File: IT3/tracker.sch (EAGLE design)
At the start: 91 parts, among them J1 THING_PLUS_PHYSICAL, Q1 2N3906, Q2 DMG6602SVT, Q3 DMG6602SVT, Q6 MMBT3906LT1SMD, Q7 DMG6602SVT, U1 ADXL343BCCZ-RL7, U2 FONA-800-BREAKOUTNOHOLE, U3 MP2155GQ-Z, U4 SPARKFUN-SWARM-M138NOTOPHOLE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

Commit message: Update 4V PSUvalues
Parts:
- R10: value 143k -> 121k
- R9: value 820k -> 845k
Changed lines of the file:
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@@
 <attribute name="VOLTAGE_RATING" value="50V"/>
 </part>
-<part name="R9" library="SparkFun-Resistors" deviceset="RESISTOR" device="0603" value=" 820k">
+<part name="R9" library="SparkFun-Resistors" deviceset="RESISTOR" device="0603" value=" 845k">
 <attribute name="TOLERANCE" value="1%"/>
 </part>
-<part name="R10" library="SparkFun-Resistors" deviceset="RESISTOR" device="0603" value="143k">
+<part name="R10" library="SparkFun-Resistors" deviceset="RESISTOR" device="0603" value="121k">
 <attribute name="TOLERANCE" value="1%"/>
 </part>

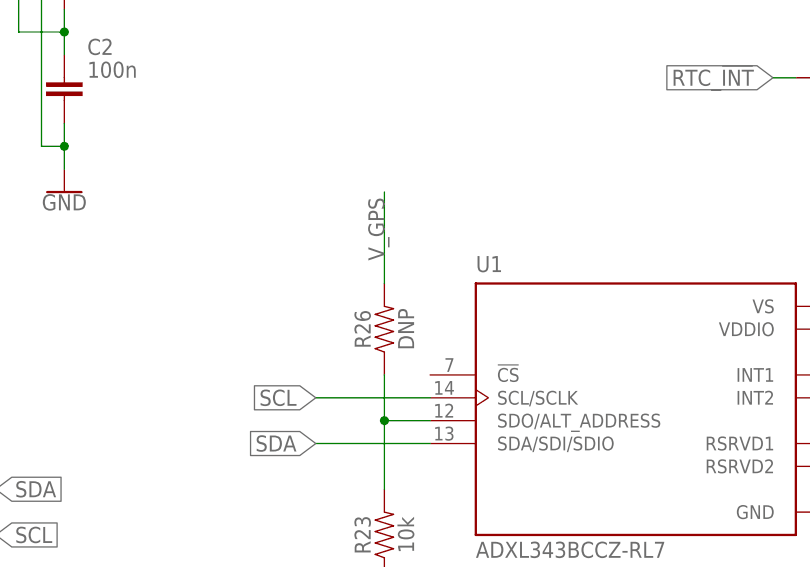
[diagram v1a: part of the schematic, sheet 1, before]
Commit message: Fixes for accelerometer CS pullup
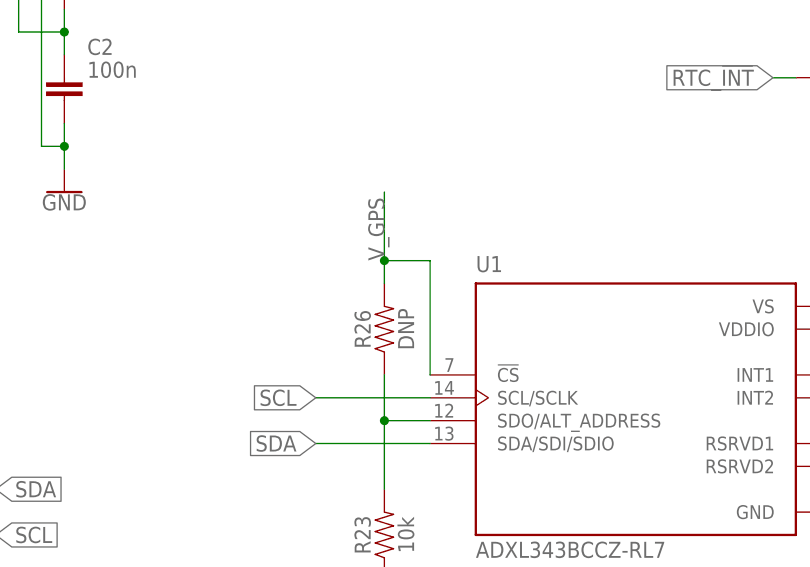
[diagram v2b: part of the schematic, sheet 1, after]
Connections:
- net V_GPS: now also U1.!CS
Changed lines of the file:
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@@
 </segment>
 <segment>
-<wire x1="129.54" y1="81.28" x2="129.54" y2="71.12" width="0.1524" layer="91"/>
+<wire x1="129.54" y1="81.28" x2="129.54" y2="73.66" width="0.1524" layer="91"/>
 <label x="129.54" y="73.66" size="1.778" layer="95" rot="R90"/>
 <pinref part="R26" gate="G$1" pin="2"/>
+<pinref part="U1" gate="G$1" pin="!CS"/>
+<wire x1="129.54" y1="73.66" x2="129.54" y2="71.12" width="0.1524" layer="91"/>
+<wire x1="134.62" y1="60.96" x2="134.62" y2="73.66" width="0.1524" layer="91"/>
+<wire x1="134.62" y1="73.66" x2="129.54" y2="73.66" width="0.1524" layer="91"/>
+<junction x="129.54" y="73.66"/>
 </segment>
 </net>

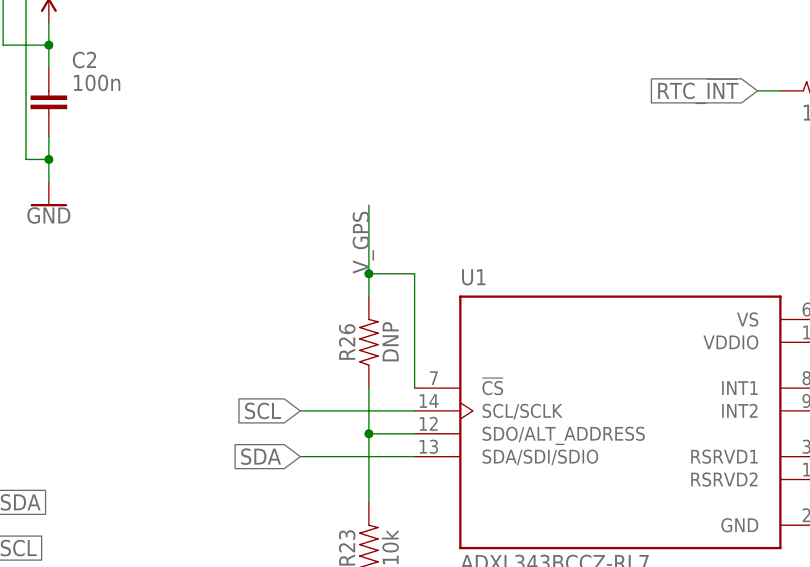
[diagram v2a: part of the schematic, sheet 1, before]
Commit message: Properly fix the accelerometer issue and move the GPS power FET slightly
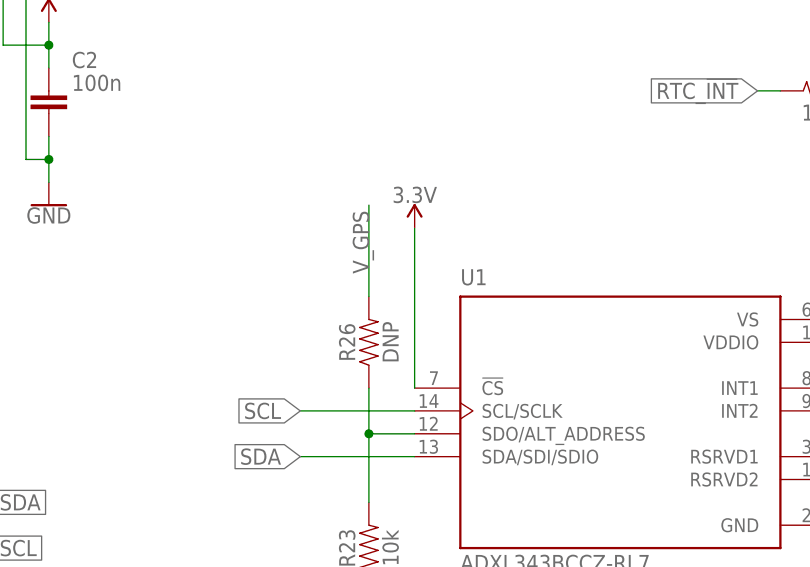
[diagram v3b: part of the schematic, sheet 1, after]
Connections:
- net 3.3V: now also U1.!CS
- net V_GPS: no longer U1.!CS
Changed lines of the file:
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@@
 <part name="GND38" library="SparkFun-PowerSymbols" deviceset="GND" device=""/>
 <part name="U$2" library="GlacTracker" deviceset="SLOT130.5" device=""/>
+<part name="SUPPLY6" library="SparkFun-PowerSymbols" deviceset="3.3V" device=""/>
 </parts>
 <sheets>
@@
 <attribute name="VALUE" x="220.98" y="27.686" size="1.778" layer="96" align="top-center"/>
 </instance>
+<instance part="SUPPLY6" gate="G$1" x="134.62" y="78.74" smashed="yes">
+<attribute name="VALUE" x="134.62" y="81.534" size="1.778" layer="96" align="bottom-center"/>
+</instance>
 </instances>
 <busses>
@@
 <pinref part="SUPPLY5" gate="G$1" pin="3.3V"/>
 <wire x1="220.98" y1="66.04" x2="220.98" y2="71.12" width="0.1524" layer="91"/>
+</segment>
+<segment>
+<pinref part="U1" gate="G$1" pin="!CS"/>
+<pinref part="SUPPLY6" gate="G$1" pin="3.3V"/>
+<wire x1="134.62" y1="60.96" x2="134.62" y2="78.74" width="0.1524" layer="91"/>
 </segment>
 </net>
@@
 </segment>
 <segment>
-<wire x1="129.54" y1="81.28" x2="129.54" y2="73.66" width="0.1524" layer="91"/>
+<wire x1="129.54" y1="81.28" x2="129.54" y2="71.12" width="0.1524" layer="91"/>
 <label x="129.54" y="73.66" size="1.778" layer="95" rot="R90"/>
 <pinref part="R26" gate="G$1" pin="2"/>
-<pinref part="U1" gate="G$1" pin="!CS"/>
-<wire x1="129.54" y1="73.66" x2="129.54" y2="71.12" width="0.1524" layer="91"/>
-<wire x1="134.62" y1="60.96" x2="134.62" y2="73.66" width="0.1524" layer="91"/>
-<wire x1="134.62" y1="73.66" x2="129.54" y2="73.66" width="0.1524" layer="91"/>
-<junction x="129.54" y="73.66"/>
-</segment>
-</net>
+</segment>
+</net>
